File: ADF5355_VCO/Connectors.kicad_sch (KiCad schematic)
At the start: 6 parts, among them J1 Conn_01x02, J2 USB_B_Micro, J3 Conn_Coaxial, J4 Conn_Coaxial, J5 Conn_Coaxial, SW3 SW_DPDT_x2

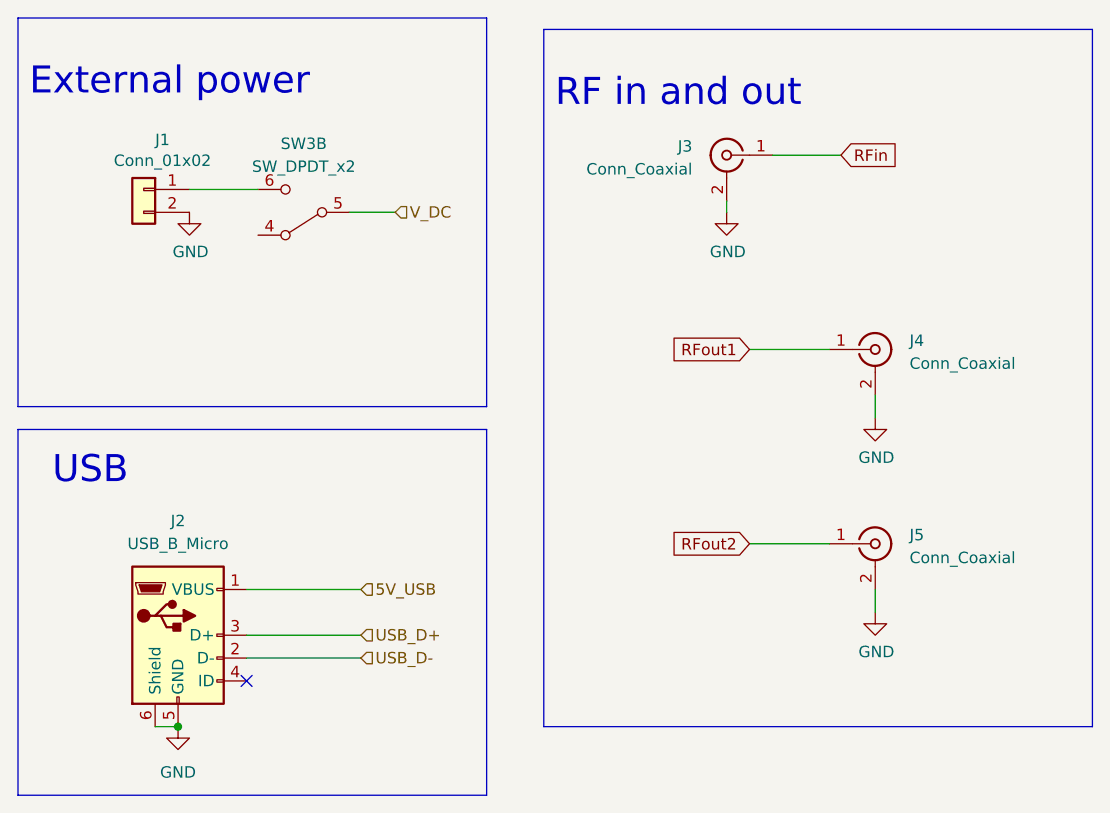
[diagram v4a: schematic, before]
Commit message: Removed the switch from power supply
Removed the switch from the main power supply and changed the switch on the boot pin to SDPT switch
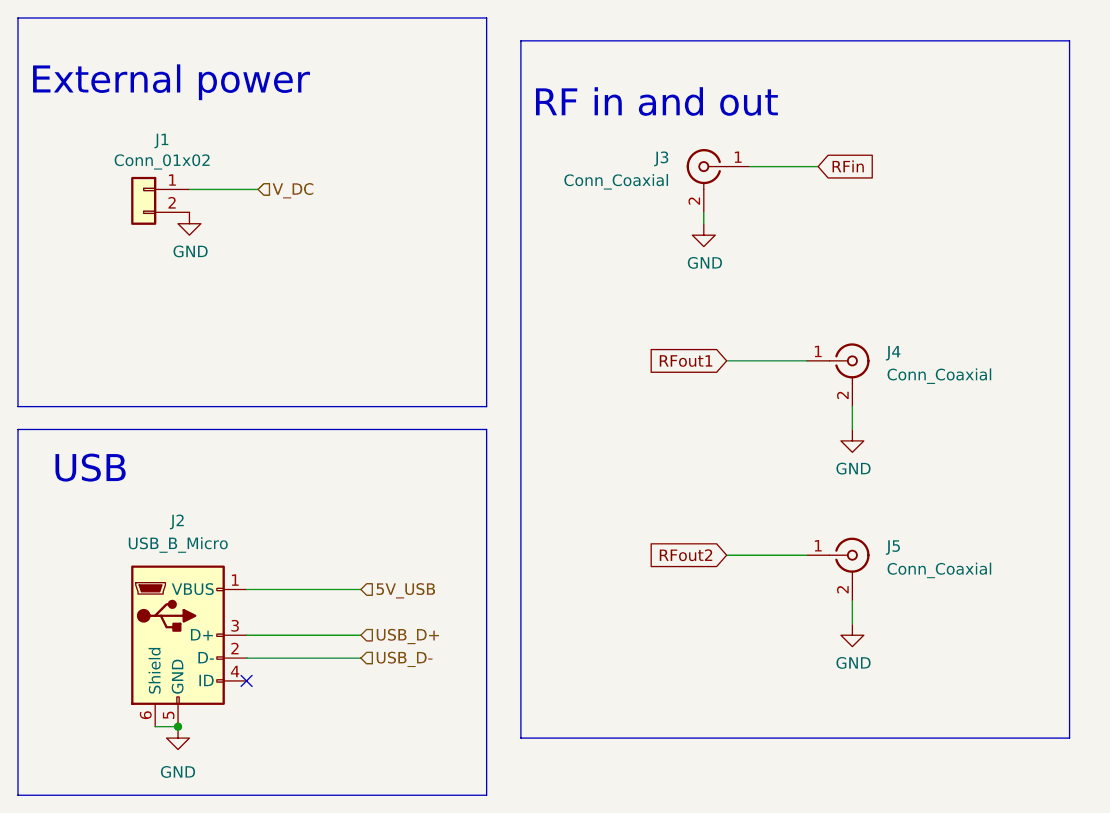
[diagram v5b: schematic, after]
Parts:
- removed SW3: SW_DPDT_x2, symbol Switch:SW_DPDT_x2
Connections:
- net V_DC: now also J1.1 (Pin_1)
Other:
- moved on the sheet: J3, J4, J5
